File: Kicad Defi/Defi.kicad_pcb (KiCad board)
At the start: 2 copper layers, 161 x 78 mm, 37 parts, among them J1 Omnimate2, J10 Autocom4, J2 Autocom2, J3 Autocom2, J4 Autocom4, J5 Mounting_Screw_3mm, J6 Mounting_Screw_3mm, J7 Mounting_Screw_3mm, J8 Autocom4, J9 Mounting_Screw_3mm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

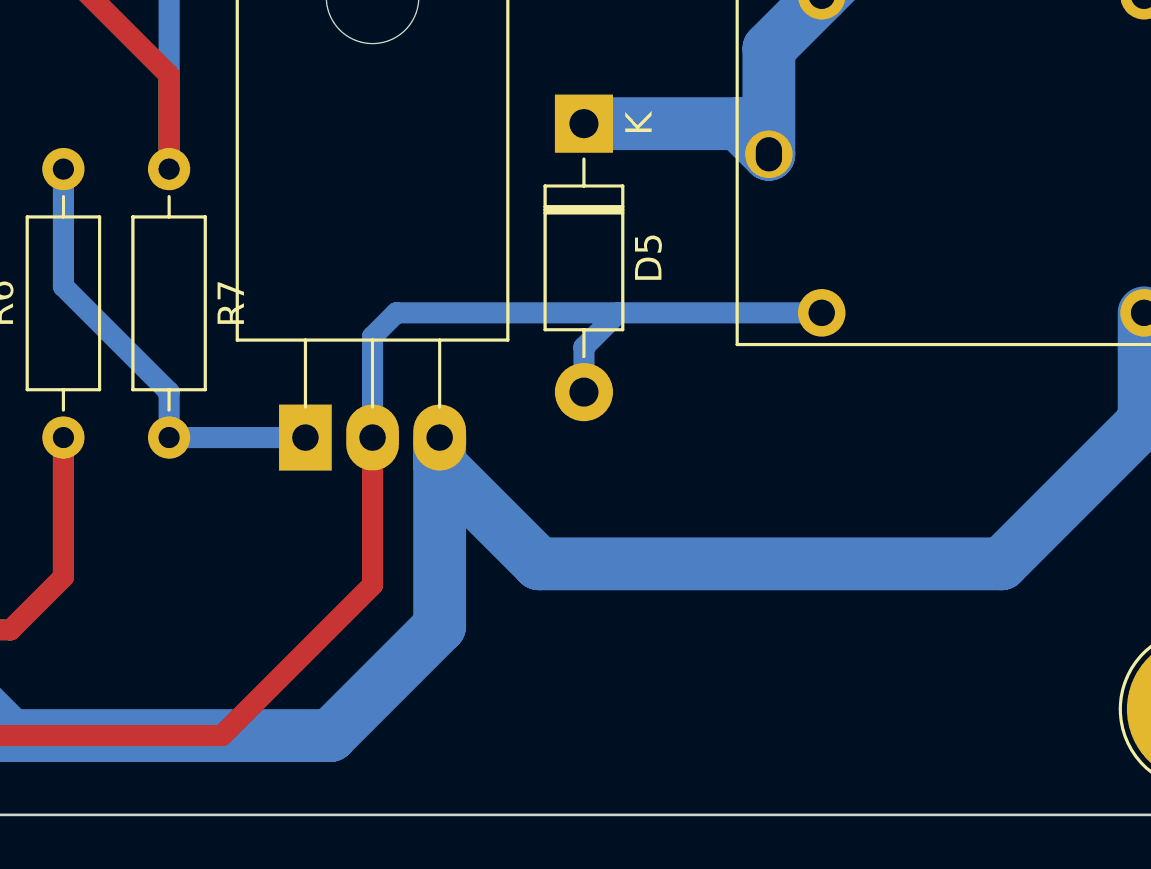
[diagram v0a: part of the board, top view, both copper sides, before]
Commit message: Mutex + LCD+ENCODEUR+MPU = test validé
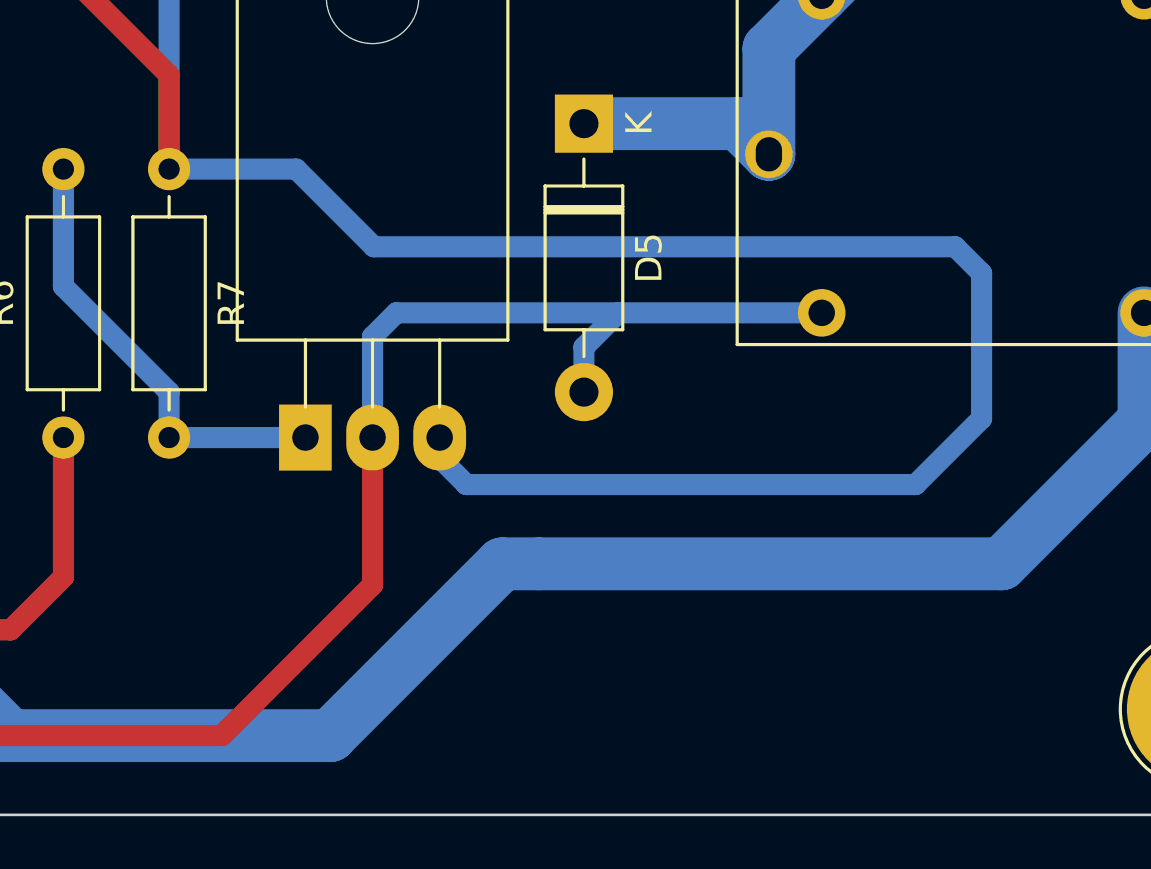
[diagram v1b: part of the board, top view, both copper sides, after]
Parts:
- R1: value 18000 -> 15k
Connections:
- Q1 pad 3: +12P -> GND
- SW1 pad 2: +12P -> GND
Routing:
- net GND: track 353.9 -> 414.6 mm
- net +12P: track 261.4 -> 253.2 mm

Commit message: Je sais plus ce que j'ai fait mais j'envoie au cas ou
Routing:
- net GND: track 414.6 -> 446.1 mm
- net +12P: track 253.2 -> 260.6 mm
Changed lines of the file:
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@@
+	)
+	(segment
+		(start 52.5 85.72)
+		(end 52.5 65.58)
+		(width 0.8)
+		(layer "B.Cu")
+		(net 2)
 	)
 	(segment
@@
 	)
 	(segment
+		(start 52.5 85.72)
+		(end 52.5 90.72)
+		(width 0.8)
+		(layer "B.Cu")
+		(net 2)
+	)
+	(segment
 		(start 48 60)
 		(end 48 61.08)
@@
 		(start 119 92)
 		(end 119 87)
+		(width 0.8)
+		(layer "B.Cu")
+		(net 2)
+	)
+	(segment
+		(start 52.5 65.58)
+		(end 48 61.08)
 		(width 0.8)
 		(layer "B.Cu")
@@
 	)
 	(segment
-		(start 55 102)
-		(end 52.5 99.5)
-		(width 2)
-		(layer "B.Cu")
-		(net 7)
-	)
-	(segment
 		(start 128 71)
 		(end 128 98)
@@
 	)
 	(segment
+		(start 44 73)
+		(end 44 100.25)
+		(width 2)
+		(layer "B.Cu")
+		(net 7)
+	)
+	(segment
 		(start 107 102)
 		(end 132 102)
@@
 	)
 	(segment
+		(start 107 102)
+		(end 56.5 102)
+		(width 2)
+		(layer "B.Cu")
+		(net 7)
+	)
+	(segment
 		(start 128 98)
 		(end 132 102)
@@
 	)
 	(segment
-		(start 107 102)
-		(end 55 102)
+		(start 45.75 102)
+		(end 56.5 102)
 		(width 2)
 		(layer "B.Cu")
@@
 	)
 	(segment
-		(start 52.5 81.5)
-		(end 44 73)
-		(width 2)
-		(layer "B.Cu")
-		(net 7)
-	)
-	(segment
-		(start 52.5 99.5)
-		(end 52.5 85.72)
-		(width 2)
-		(layer "B.Cu")
-		(net 7)
-	)
-	(segment
-		(start 52.5 85.72)
-		(end 52.5 81.5)
+		(start 44 100.25)
+		(end 45.75 102)
 		(width 2)
 		(layer "B.Cu")
@@
 	)
 	(segment
+		(start 56.5 102)
+		(end 54.5 102)
+		(width 2)
+		(layer "B.Cu")
+		(net 7)
+	)
+	(segment
 		(start 74.195 90.72)
 		(end 75.46 91.985)
@@
 	)
 	(segment
+		(start 145.7 96.3)
+		(end 145.7 90.72)
+		(width 0.8)
+		(layer "F.Cu")
+		(net 10)
+	)
+	(segment
 		(start 47.5 100.5)
 		(end 47.5 99)
@@
 		(start 140 102)
 		(end 49 102)
-		(width 0.8)
-		(layer "F.Cu")
-		(net 10)
-	)
-	(segment
-		(start 145.7 90.72)
-		(end 145.7 96.3)
 		(width 0.8)
 		(layer "F.Cu")
@@
 	)
 	(segment
+		(start 155 86)
+		(end 146.6 86)
+		(width 0.8)
+		(layer "B.Cu")
+		(net 10)
+	)
+	(segment
 		(start 145.7 86.9)
 		(end 145.7 90.72)
 		(width 0.8)
 		(layer "B.Cu")
-		(net 10)
-	)
-	(segment
-		(start 155 86)
-		(end 146.6 86)
-		(width 0.8)
-		(layer "B.Cu")
